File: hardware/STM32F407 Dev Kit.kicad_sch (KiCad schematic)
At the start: 0 parts

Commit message: Design schematic for MIC & Headphones
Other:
- added sheet [6] - ADC (adc_6.kicad_sch)
- added sheet [7] - DAC & Mic (dac_mic_7.kicad_sch)
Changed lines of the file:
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@@
 	)
 	(sheet
-		(at 20.32 17.78)
-		(size 76.2 33.02)
+		(at 20.32 24.13)
+		(size 50.8 50.8)
 		(exclude_from_sim no)
 		(in_bom yes)
@@
 		)
 		(property "Sheetname" "[1] - Block Diagram"
-			(at 20.32 17.0684 0)
+			(at 20.32 23.4184 0)
 			(show_name no)
 			(do_not_autoplace no)
@@
 		)
 		(property "Sheetfile" "block_diagram_1.kicad_sch"
-			(at 20.32 51.3846 0)
+			(at 20.32 75.5146 0)
 			(show_name no)
 			(do_not_autoplace no)
@@
 	)
 	(sheet
-		(at 26.162 76.708)
-		(size 49.53 50.546)
+		(at 226.06 24.13)
+		(size 49.53 50.8)
 		(exclude_from_sim no)
 		(in_bom yes)
@@
 		)
 		(property "Sheetname" "[4] - ETHERNET PHY"
-			(at 26.162 75.9964 0)
+			(at 226.06 23.4184 0)
 			(show_name no)
 			(do_not_autoplace no)
@@
 		)
 		(property "Sheetfile" "ethernet_phy_4.kicad_sch"
-			(at 26.162 127.8386 0)
+			(at 226.06 75.5146 0)
 			(show_name no)
 			(do_not_autoplace no)
@@
 	)
 	(sheet
-		(at 111.76 17.78)
-		(size 72.39 33.02)
+		(at 154.94 101.6)
+		(size 50.8 50.8)
+		(exclude_from_sim no)
+		(in_bom yes)
+		(on_board yes)
+		(dnp no)
+		(fields_autoplaced yes)
+		(stroke
+			(width 0.1524)
+			(type solid)
+		)
+		(fill
+			(color 0 0 0 0)
+		)
+		(property "Sheetname" "[7] - DAC & Mic"
+			(at 154.94 100.8884 0)
+			(show_name no)
+			(do_not_autoplace no)
+			(effects
+				(font
+					(size 1.27 1.27)
+				)
+				(justify left bottom)
+			)
+		)
+		(property "Sheetfile" "dac_mic_7.kicad_sch"
+			(at 154.94 152.9846 0)
+			(show_name no)
+			(do_not_autoplace no)
+			(effects
+				(font
+					(size 1.27 1.27)
+				)
+				(justify left top)
+			)
+		)
+		(instances
+			(project "STM32F407 Dev Kit"
+				(path "/f3d27387-fbda-4c9d-aea0-93d92d34cd17"
+					(page "8")
+				)
+			)
+		)
+	)
+	(sheet
+		(at 87.63 25.4)
+		(size 50.8 50.8)
 		(exclude_from_sim no)
 		(in_bom yes)
@@
 		)
 		(property "Sheetname" "[2] - Power Budget"
-			(at 111.76 17.0684 0)
+			(at 87.63 24.6884 0)
 			(show_name no)
 			(do_not_autoplace no)
@@
 		)
 		(property "Sheetfile" "power_budget_2.kicad_sch"
-			(at 111.76 51.3846 0)
+			(at 87.63 76.7846 0)
 			(show_name no)
 			(do_not_autoplace no)
@@
 	)
 	(sheet
-		(at 194.31 17.78)
-		(size 69.85 27.94)
+		(at 154.94 25.4)
+		(size 50.8 50.8)
 		(exclude_from_sim no)
 		(in_bom yes)
@@
 		)
 		(property "Sheetname" "[3] - STM32F103 debugger"
-			(at 194.31 17.0684 0)
+			(at 154.94 24.6884 0)
 			(show_name no)
 			(do_not_autoplace no)
@@
 		)
 		(property "Sheetfile" "stm32f103_debugger_3.kicad_sch"
-			(at 194.31 46.3046 0)
+			(at 154.94 76.7846 0)
 			(show_name no)
 			(do_not_autoplace no)
@@
 	)
 	(sheet
-		(at 95.25 77.47)
-		(size 91.44 33.02)
+		(at 20.828 101.092)
+		(size 50.8 50.8)
 		(exclude_from_sim no)
 		(in_bom yes)
@@
 		)
 		(property "Sheetname" "[5] - Motor Driver"
-			(at 95.25 76.7584 0)
+			(at 20.828 100.3804 0)
 			(show_name no)
 			(do_not_autoplace no)
@@
 		)
 		(property "Sheetfile" "motor_driver_5.kicad_sch"
-			(at 95.25 111.0746 0)
+			(at 20.828 152.4766 0)
 			(show_name no)
 			(do_not_autoplace no)
@@
 				)
 			)
+		)
+	)
+	(sheet
+		(at 87.63 101.6)
+		(size 50.8 50.8)
+		(exclude_from_sim no)
+		(in_bom yes)
+		(on_board yes)
+		(dnp no)
+		(fields_autoplaced yes)
+		(stroke
+			(width 0.1524)
+			(type solid)
+		)
+		(fill
+			(color 0 0 0 0)
+		)
+		(property "Sheetname" "[6] - ADC"
+			(at 87.63 100.8884 0)
+			(show_name no)
+			(do_not_autoplace no)
+			(effects
+				(font
+					(size 1.27 1.27)
+				)
+				(justify left bottom)
+			)
+		)
+		(property "Sheetfile" "adc_6.kicad_sch"
+			(at 87.63 152.9846 0)
+			(show_name no)
+			(do_not_autoplace no)
+			(effects
+				(font
+					(size 1.27 1.27)
+				)
+				(justify left top)
+			)
+		)
+		(instances
+			(project "STM32F407 Dev Kit"
+				(path "/f3d27387-fbda-4c9d-aea0-93d92d34cd17"
+					(page "7")
+				)
+			)

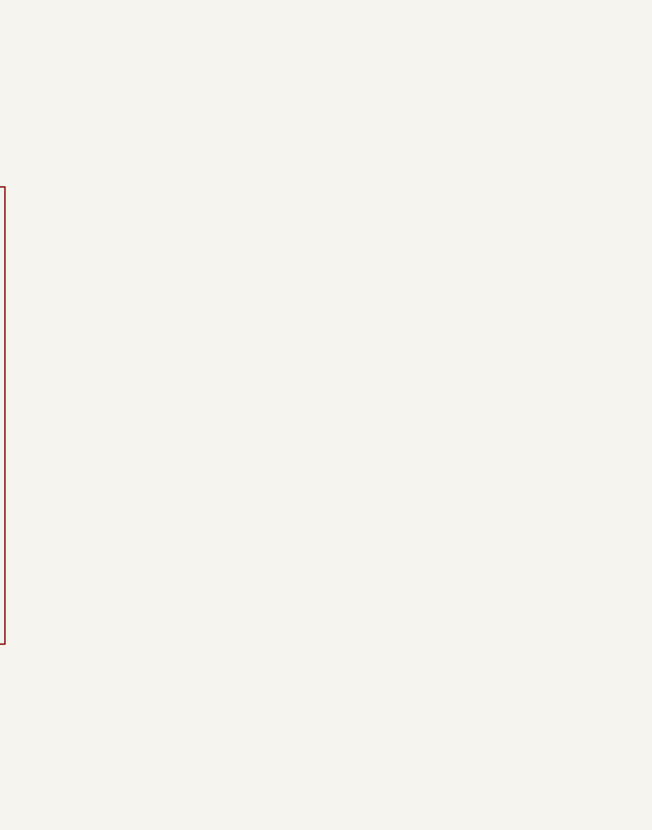
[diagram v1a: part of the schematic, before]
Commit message: Design Schematic for STM32F407
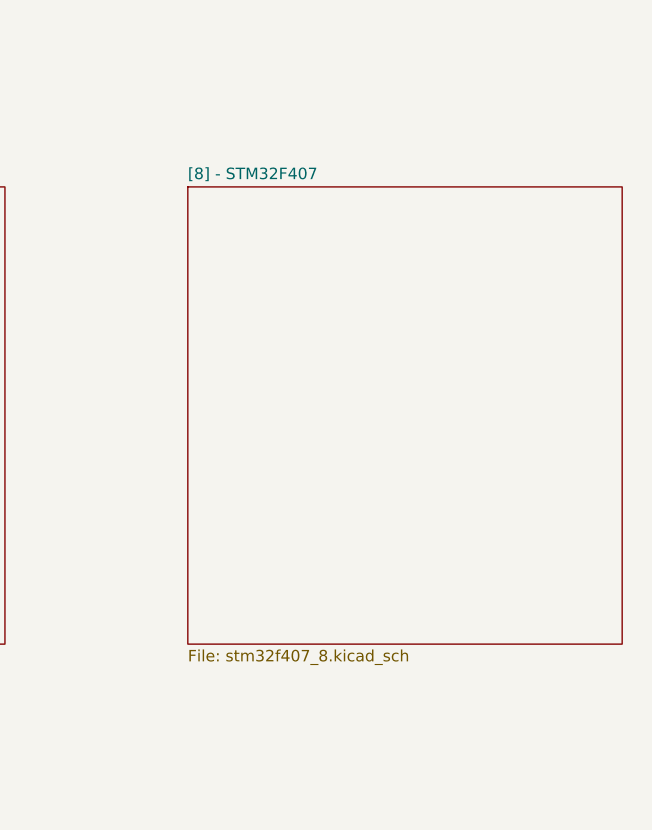
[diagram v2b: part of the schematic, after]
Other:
- added sheet [8] - STM32F407 (stm32f407_8.kicad_sch)
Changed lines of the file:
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@@
+	)
+	(sheet
+		(at 226.06 101.6)
+		(size 48.26 50.8)
+		(exclude_from_sim no)
+		(in_bom yes)
+		(on_board yes)
+		(dnp no)
+		(fields_autoplaced yes)
+		(stroke
+			(width 0.1524)
+			(type solid)
+		)
+		(fill
+			(color 0 0 0 0)
+		)
+		(property "Sheetname" "[8] - STM32F407"
+			(at 226.06 100.8884 0)
+			(show_name no)
+			(do_not_autoplace no)
+			(effects
+				(font
+					(size 1.27 1.27)
+				)
+				(justify left bottom)
+			)
+		)
+		(property "Sheetfile" "stm32f407_8.kicad_sch"
+			(at 226.06 152.9846 0)
+			(show_name no)
+			(do_not_autoplace no)
+			(effects
+				(font
+					(size 1.27 1.27)
+				)
+				(justify left top)
+			)
+		)
+		(instances
+			(project "STM32F407 Dev Kit"
+				(path "/f3d27387-fbda-4c9d-aea0-93d92d34cd17"
+					(page "9")
+				)
+			)
+		)
 	)
 	(sheet

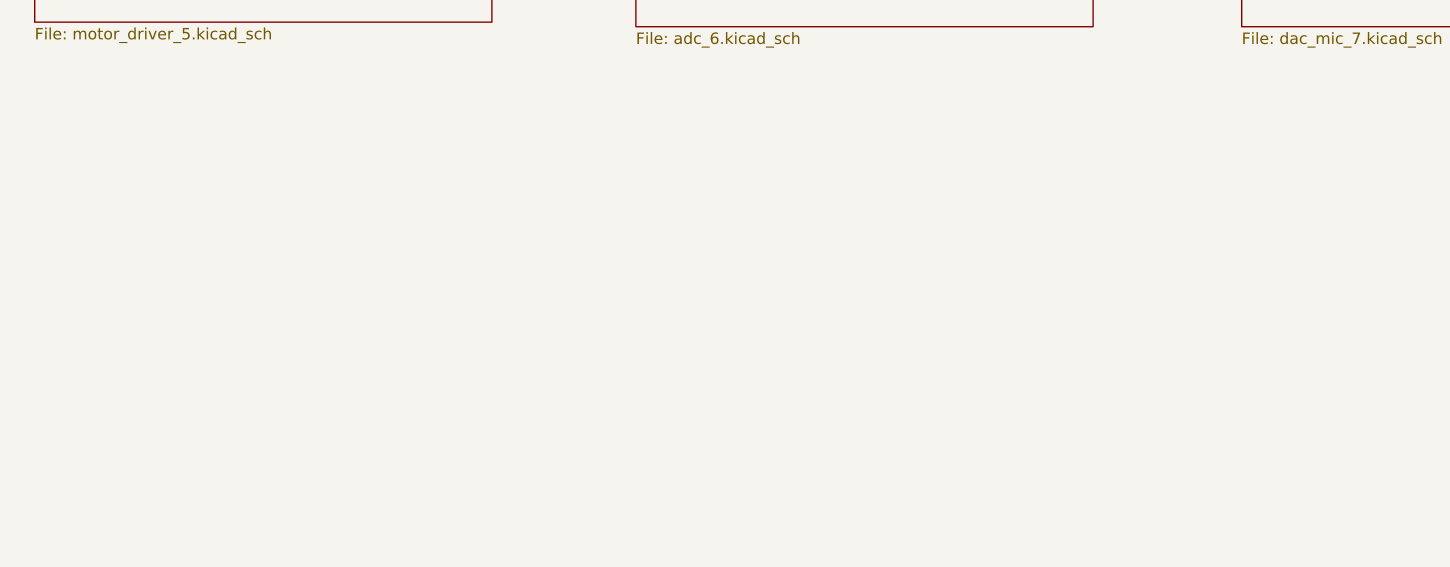
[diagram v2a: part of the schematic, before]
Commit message: Complete Schematic for Power Section
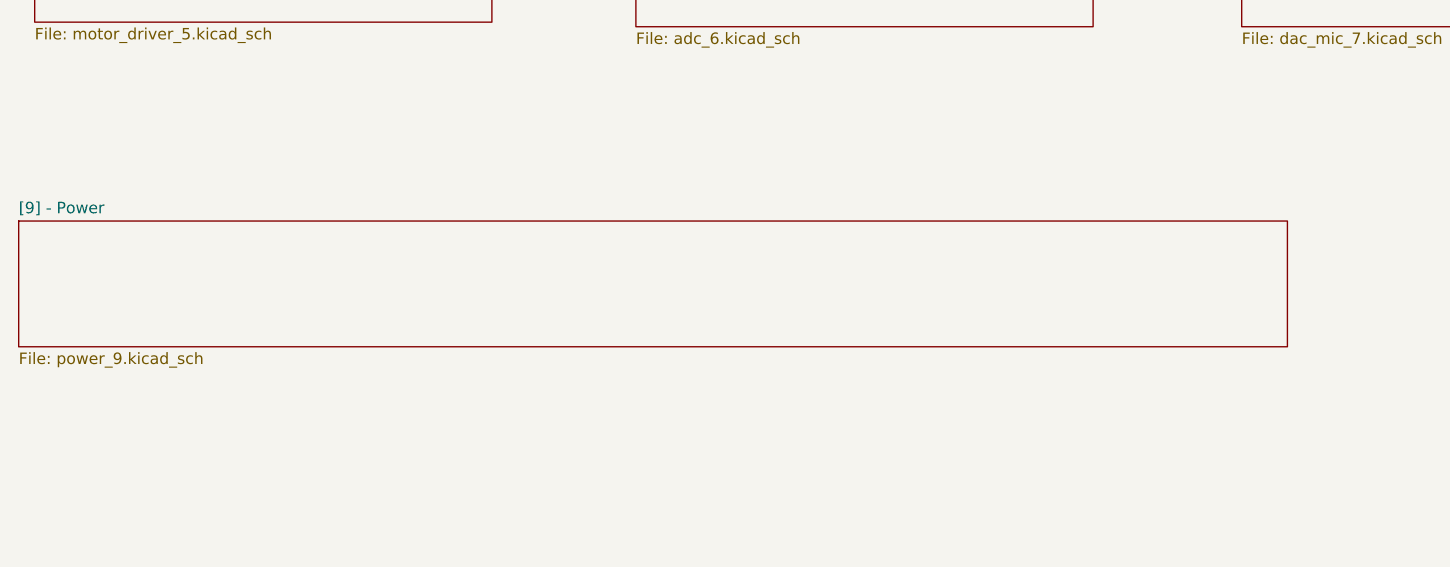
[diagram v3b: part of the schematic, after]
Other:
- added sheet [9] - Power (power_9.kicad_sch)
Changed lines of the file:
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@@
+	)
+	(sheet
+		(at 19.05 173.99)
+		(size 140.97 13.97)
+		(exclude_from_sim no)
+		(in_bom yes)
+		(on_board yes)
+		(dnp no)
+		(fields_autoplaced yes)
+		(stroke
+			(width 0.1524)
+			(type solid)
+		)
+		(fill
+			(color 0 0 0 0)
+		)
+		(property "Sheetname" "[9] - Power"
+			(at 19.05 173.2784 0)
+			(show_name no)
+			(do_not_autoplace no)
+			(effects
+				(font
+					(size 1.27 1.27)
+				)
+				(justify left bottom)
+			)
+		)
+		(property "Sheetfile" "power_9.kicad_sch"
+			(at 19.05 188.5446 0)
+			(show_name no)
+			(do_not_autoplace no)
+			(effects
+				(font
+					(size 1.27 1.27)
+				)
+				(justify left top)
+			)
+		)
+		(instances
+			(project "STM32F407 Dev Kit"
+				(path "/f3d27387-fbda-4c9d-aea0-93d92d34cd17"
+					(page "10")
+				)
+			)
+		)
 	)
 	(sheet

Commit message: Organize schematic
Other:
- sheet [4] - ETHERNET PHY renamed [4] - Ethernet PHY
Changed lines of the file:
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@@
 			(color 0 0 0 0)
 		)
-		(property "Sheetname" "[4] - ETHERNET PHY"
+		(property "Sheetname" "[4] - Ethernet PHY"
 			(at 226.06 23.4184 0)
 			(show_name no)
